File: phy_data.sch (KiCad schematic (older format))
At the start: 10 parts

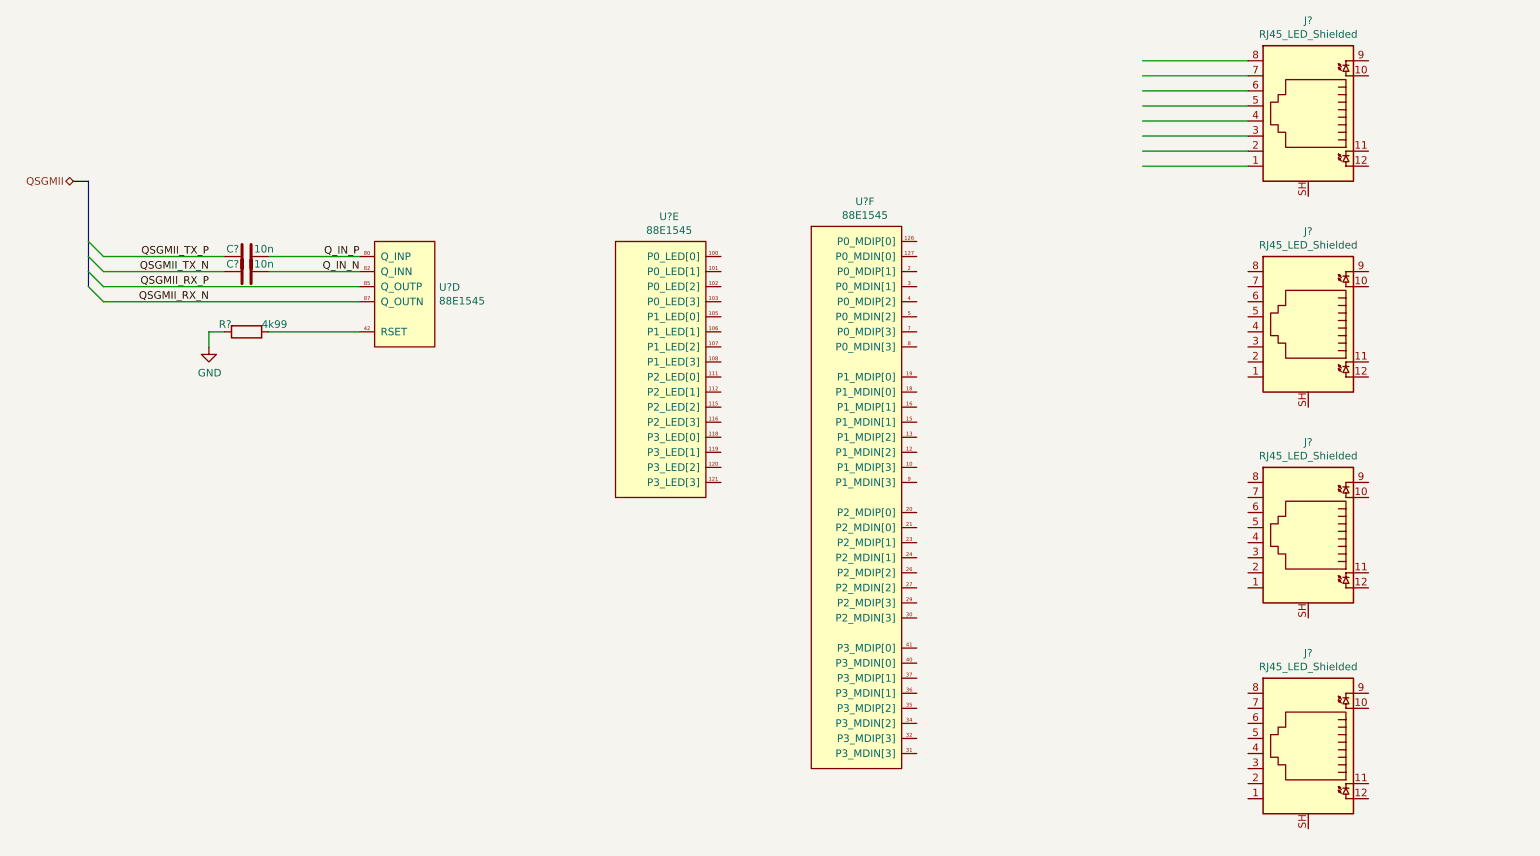
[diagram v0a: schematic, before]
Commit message: sch: Done phy data plane
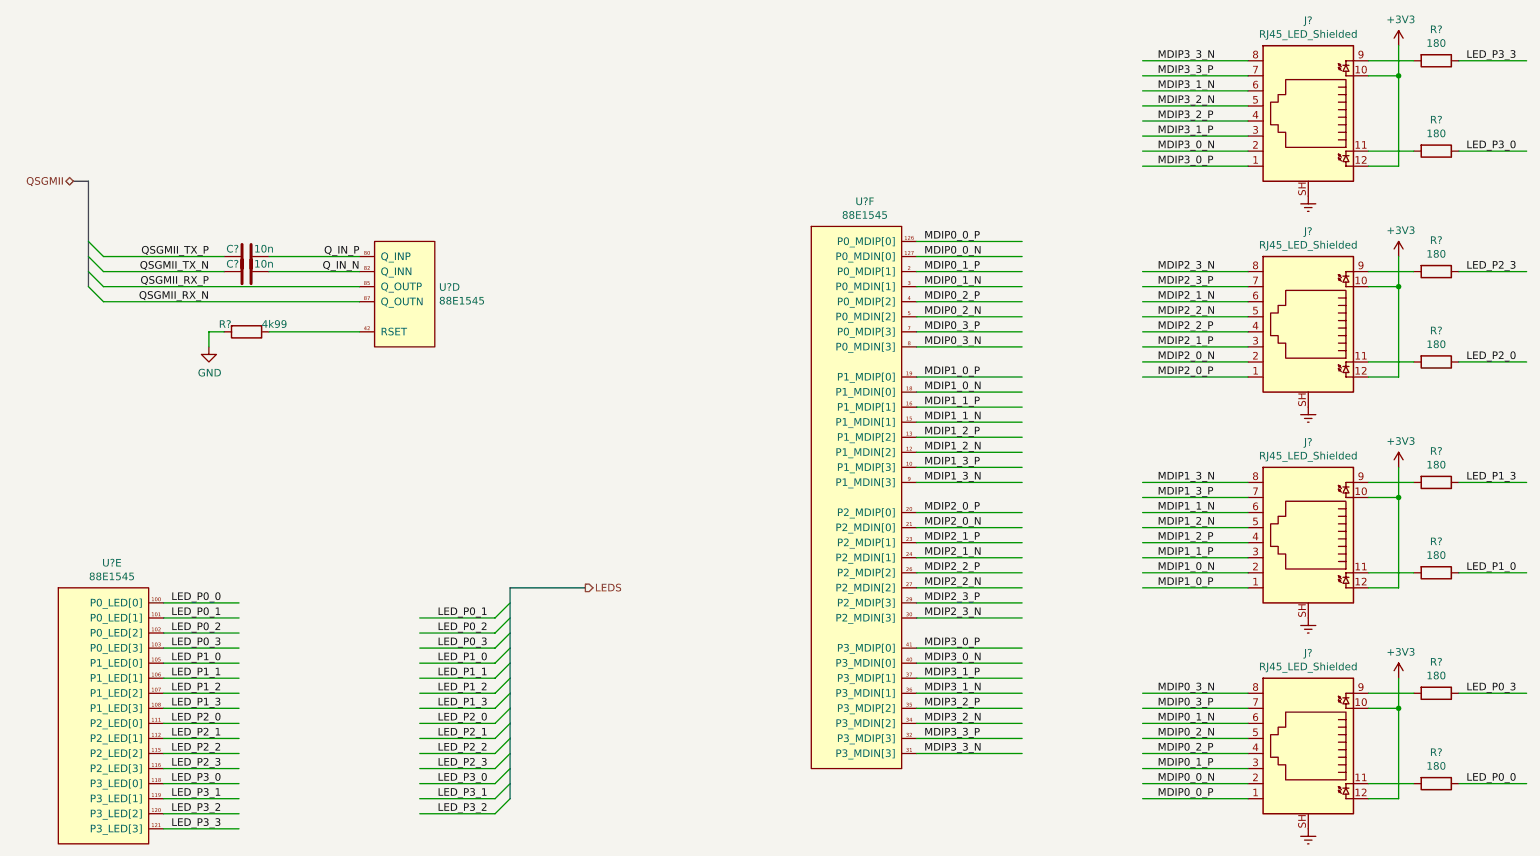
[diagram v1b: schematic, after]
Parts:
- added R? (x8): 180, symbol Device:R
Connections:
- net labels added: +3V3, Earth, LEDS, LED_P0_0, LED_P0_1, LED_P0_2, LED_P0_3, LED_P1_0, LED_P1_1, LED_P1_2, LED_P1_3, LED_P2_0, LED_P2_1, LED_P2_2, LED_P2_3, LED_P3_0, LED_P3_1, LED_P3_2, LED_P3_3, MDIP0_0_N, MDIP0_0_P, MDIP0_1_N, MDIP0_1_P, MDIP0_2_N, MDIP0_2_P, MDIP0_3_N, MDIP0_3_P, MDIP1_0_N, MDIP1_0_P, MDIP1_1_N, MDIP1_1_P, MDIP1_2_N, MDIP1_2_P, MDIP1_3_N, MDIP1_3_P, MDIP2_0_N, MDIP2_0_P, MDIP2_1_N, MDIP2_1_P, MDIP2_2_N, MDIP2_2_P, MDIP2_3_N, MDIP2_3_P, MDIP3_0_N, MDIP3_0_P, MDIP3_1_N, MDIP3_1_P, MDIP3_2_N, MDIP3_2_P, MDIP3_3_N, MDIP3_3_P
- wire segments 17 -> 135
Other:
- moved on the sheet: U?E
